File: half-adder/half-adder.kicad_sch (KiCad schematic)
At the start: 14 parts, among them J1 A, J2 B, J3 C, J4 5V, J5 GROUND, J6 CARRY OUT, J7 OUTPUT

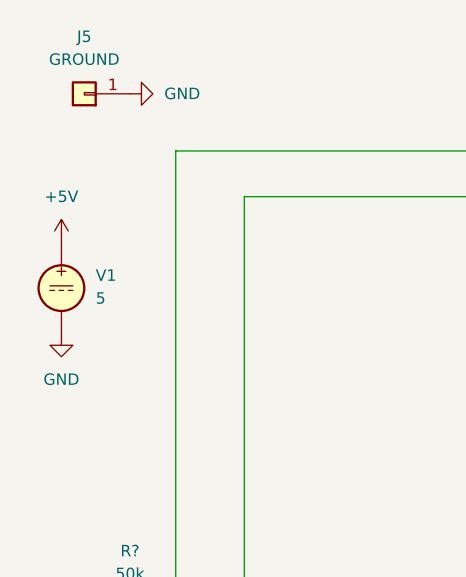
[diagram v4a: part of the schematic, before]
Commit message: complete 2-bit encoder
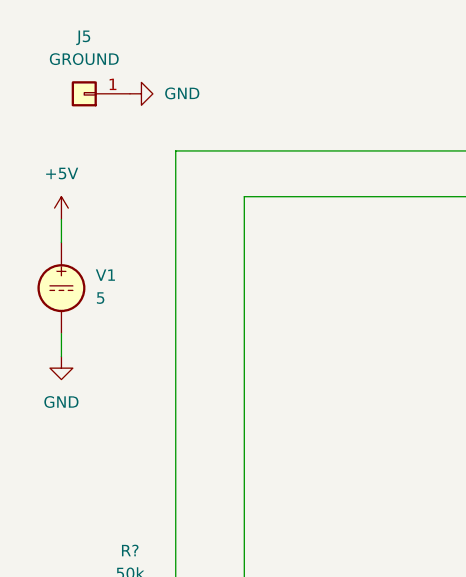
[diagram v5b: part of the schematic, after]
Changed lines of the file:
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@@
+	(wire
+		(pts
+			(xy 17.78 64.77) (xy 17.78 62.23)
+		)
+		(stroke
+			(width 0)
+			(type default)
+		)
+	)
 	(wire
 		(pts
@@
 		(pts
 			(xy 24.13 139.7) (xy 25.4 139.7)
+		)
+		(stroke
+			(width 0)
+			(type default)
+		)
+	)
+	(wire
+		(pts
+			(xy 17.78 49.53) (xy 17.78 52.07)
 		)
 		(stroke
@@
 	(symbol
 		(lib_id "power:+5V")
-		(at 17.78 52.07 0)
+		(at 17.78 49.53 0)
 		(unit 1)
 		(exclude_from_sim no)
@@
 		(fields_autoplaced yes)
 		(property "Reference" "#PWR01"
-			(at 17.78 55.88 0)
+			(at 17.78 53.34 0)
 			(effects
 				(font
@@
 		)
 		(property "Value" "+5V"
-			(at 17.78 46.99 0)
+			(at 17.78 44.45 0)
 			(effects
 				(font
@@
 		)
 		(property "Footprint" ""
-			(at 17.78 52.07 0)
+			(at 17.78 49.53 0)
 			(effects
 				(font
@@
 		)
 		(property "Datasheet" ""
-			(at 17.78 52.07 0)
-			(effects
-				(font
-					(size 1.27 1.27)
-				)
-				(hide yes)
-			)
-		)
-		(property "Description" ""
-			(at 17.78 52.07 0)
+			(at 17.78 49.53 0)
+			(effects
+				(font
+					(size 1.27 1.27)
+				)
+				(hide yes)
+			)
+		)
+		(property "Description" "Power symbol creates a global label with name \"+5V\""
+			(at 17.78 49.53 0)
 			(effects
 				(font
@@
 	)
 	(symbol
-		(lib_name "GND_1")
 		(lib_id "power:GND")
 		(at 25.4 132.08 0)
@@
 			)
 		)
-		(property "Datasheet" "~"
+		(property "Datasheet" "https://ngspice.sourceforge.io/docs/ngspice-html-manual/manual.xhtml#sec_Independent_Sources_for"
 			(at 17.78 57.15 0)
 			(effects
@@
 			)
 		)
-		(property "Description" ""
+		(property "Description" "Voltage source, DC"
 			(at 17.78 57.15 0)
 			(effects
@@
 			)
 		)
-		(property "Description" ""
+		(property "Description" "Power symbol creates a global label with name \"GND\" , ground"
 			(at 50.8 132.08 0)
 			(effects
@@
 			)
 		)
-		(property "Description" ""
+		(property "Description" "Power symbol creates a global label with name \"GND\" , ground"
 			(at 45.72 110.49 0)
 			(effects
@@
 			)
 		)
-		(property "Description" ""
+		(property "Description" "Power symbol creates a global label with name \"GND\" , ground"
 			(at 21.59 92.71 0)
 			(effects
@@
 	)
 	(symbol
-		(lib_name "GND_1")
 		(lib_id "power:GND")
 		(at 25.4 114.3 0)
@@
 	(symbol
 		(lib_id "power:GND")
-		(at 17.78 62.23 0)
+		(at 17.78 64.77 0)
 		(unit 1)
 		(exclude_from_sim no)
@@
 		(fields_autoplaced yes)
 		(property "Reference" "#PWR02"
-			(at 17.78 68.58 0)
+			(at 17.78 71.12 0)
 			(effects
 				(font
@@
 		)
 		(property "Value" "GND"
-			(at 17.78 67.31 0)
+			(at 17.78 69.85 0)
 			(effects
 				(font
@@
 		)
 		(property "Footprint" ""
-			(at 17.78 62.23 0)
+			(at 17.78 64.77 0)
 			(effects
 				(font
@@
 		)
 		(property "Datasheet" ""
-			(at 17.78 62.23 0)
-			(effects
-				(font
-					(size 1.27 1.27)
-				)
-				(hide yes)
-			)
-		)
-		(property "Description" ""
-			(at 17.78 62.23 0)
+			(at 17.78 64.77 0)
+			(effects
+				(font
+					(size 1.27 1.27)
+				)
+				(hide yes)
+			)
+		)
+		(property "Description" "Power symbol creates a global label with name \"GND\" , ground"
+			(at 17.78 64.77 0)
 			(effects
 				(font
@@
 			)
 		)
-		(property "Description" ""
+		(property "Description" "Power symbol creates a global label with name \"+5V\""
 			(at 25.4 22.86 0)
 			(effects
@@
 			)
 		)
-		(property "Description" ""
+		(property "Description" "Power symbol creates a global label with name \"+5V\""
 			(at 128.27 21.59 0)
 			(effects
@@
 			)
 		)
-		(property "Description" ""
+		(property "Description" "Special symbol for telling ERC where power comes from"
 			(at 128.27 21.59 0)
 			(effects
@@
 			)
 		)
-		(property "Description" ""
+		(property "Description" "Special symbol for telling ERC where power comes from"
 			(at 142.24 21.59 0)
 			(effects
@@
 	)
 	(symbol
-		(lib_name "GND_1")
 		(lib_id "power:GND")
 		(at 25.4 152.4 0)
@@
 			)
 		)
-		(property "Description" ""
+		(property "Description" "Power symbol creates a global label with name \"GND\" , ground"
 			(at 142.24 21.59 0)
 			(effects
@@
 			)
 		)
-		(property "Description" ""
+		(property "Description" "Power symbol creates a global label with name \"GND\" , ground"
 			(at 25.4 35.56 0)
 			(effects

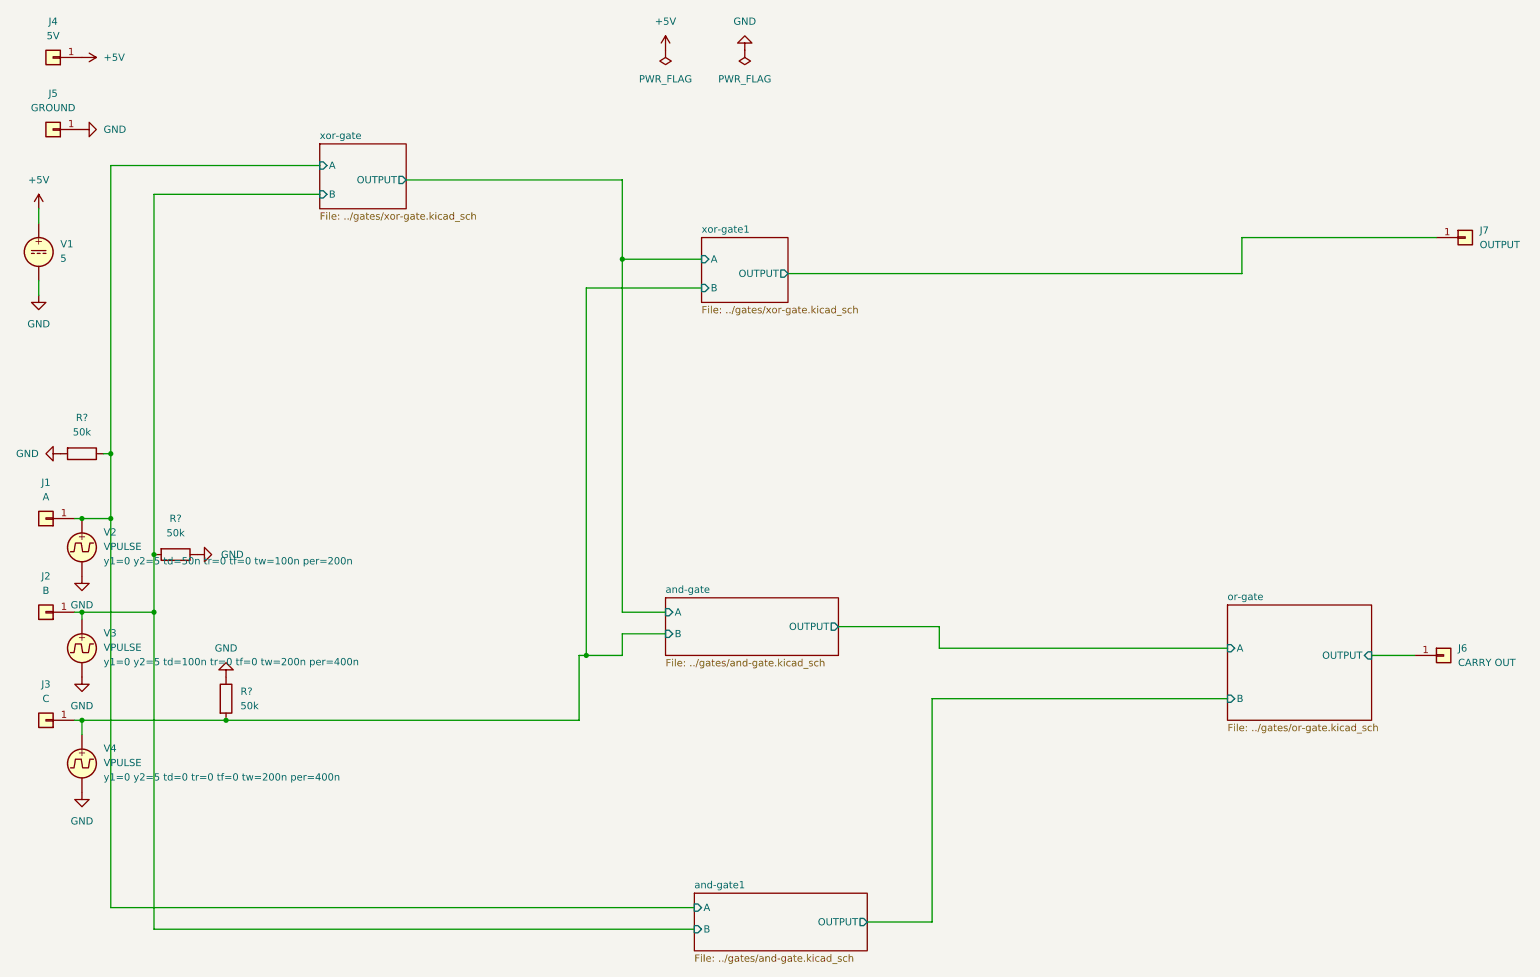
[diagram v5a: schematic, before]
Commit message: Use IC circuits in adder circuit
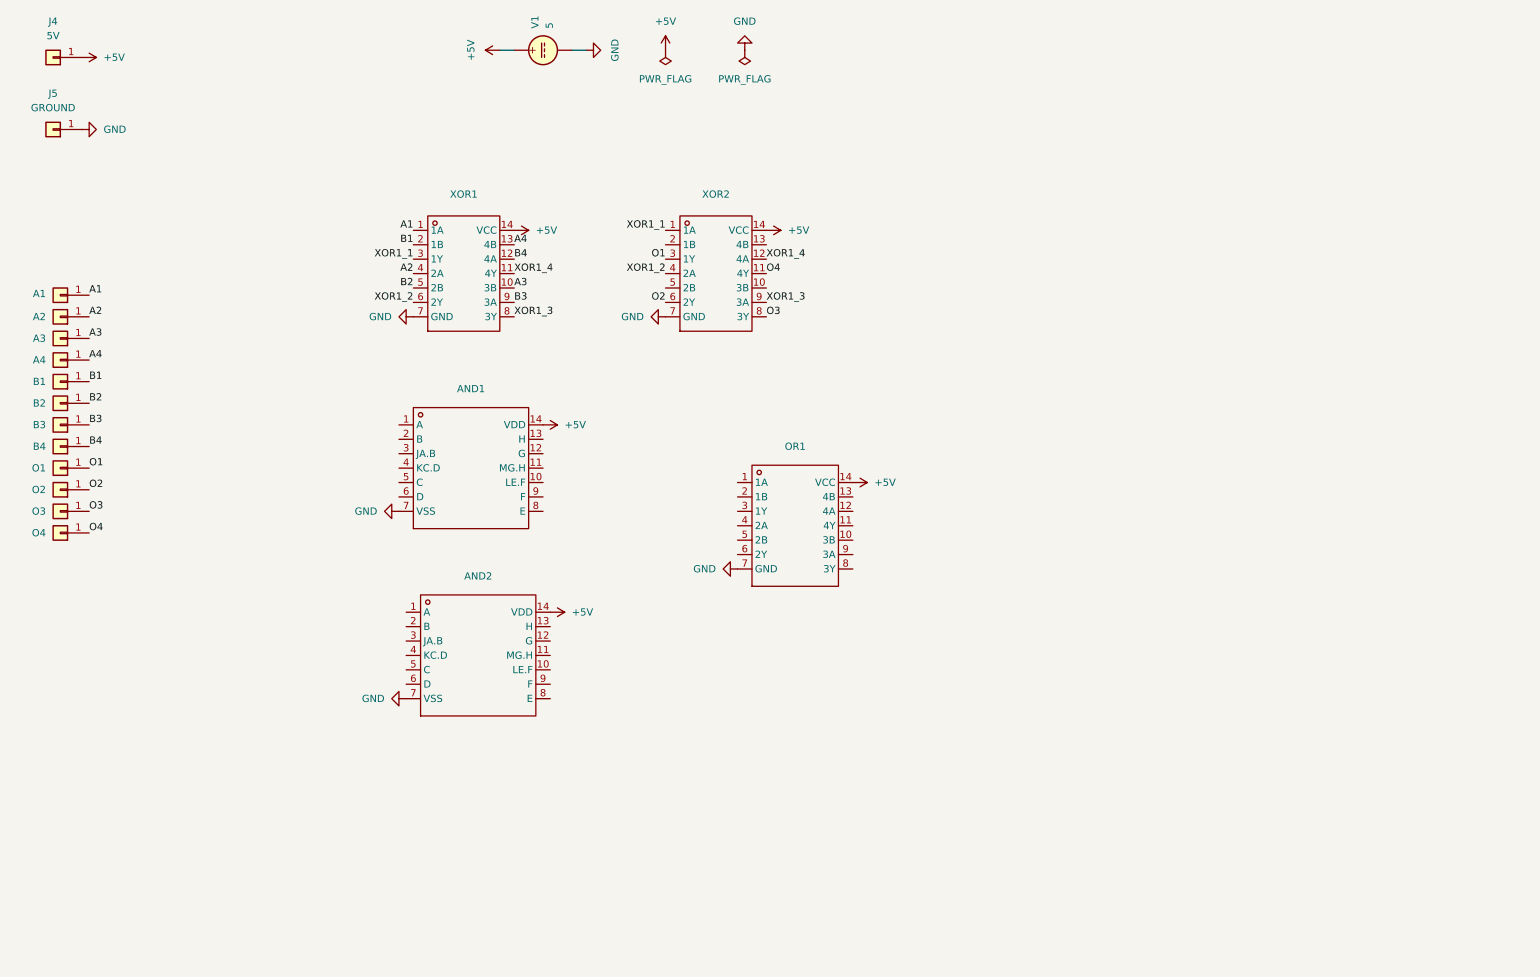
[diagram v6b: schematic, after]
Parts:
- removed J1: A, Connector_PinHeader_2.54mm:PinHeader_1x01_P2.54mm_Vertical, symbol Connector_Generic:Conn_01x01
- removed J2: B, Connector_PinHeader_2.54mm:PinHeader_1x01_P2.54mm_Vertical, symbol Connector_Generic:Conn_01x01
- removed J3: C, Connector_PinHeader_2.54mm:PinHeader_1x01_P2.54mm_Vertical, symbol Connector_Generic:Conn_01x01
- removed J6: CARRY OUT, Connector_PinHeader_2.54mm:PinHeader_1x01_P2.54mm_Vertical, symbol Connector_Generic:Conn_01x01
- removed J7: OUTPUT, Connector_PinHeader_2.54mm:PinHeader_1x01_P2.54mm_Vertical, symbol Connector_Generic:Conn_01x01
- removed R? (x3): 50k, R0603:R0603, symbol Device:R
- removed V2, V3, V4: VPULSE, symbol Simulation_SPICE:VPULSE
- added A1, A2, A3, A4, B1, B2, B3, B4, O1, O2, O3, O4: ~, Connector_PinHeader_2.54mm:PinHeader_1x01_P2.54mm_Vertical, symbol Connector_Generic:Conn_01x01
- added AND1, AND2: ~, easyeda:PDIP-14_L19.3-W6.4-P2.54-LS7.6-BL, symbol easyeda:CD4081BE
- added OR1: ~, easyeda:DIP-14_L19.0-W7.0-P2.54-LS7.6-BL, symbol easyeda:SN74HC32N
- added XOR1, XOR2: ~, easyeda:SOIC-14_L8.7-W3.9-P1.27-LS6.0-BL, symbol easyeda:74HC86D
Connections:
- net +5V: now also AND1.14 (VDD), AND2.14 (VDD), OR1.14 (VCC), XOR1.14 (VCC), XOR2.14 (VCC)
- net GND: now also AND1.7 (VSS), AND2.7 (VSS), OR1.7 (GND), XOR1.7 (GND), XOR2.7 (GND)
- new net A1: A1.1 (Pin_1), XOR1.1 (1A)
- new net A2: A2.1 (Pin_1), XOR1.4 (2A)
- new net A3: A3.1 (Pin_1), XOR1.10 (3B)
- new net A4: A4.1 (Pin_1), XOR1.13 (4B)
- new net B1: B1.1 (Pin_1), XOR1.2 (1B)
- new net B2: B2.1 (Pin_1), XOR1.5 (2B)
- new net B3: B3.1 (Pin_1), XOR1.9 (3A)
- new net B4: B4.1 (Pin_1), XOR1.12 (4A)
- new net O1: O1.1 (Pin_1), XOR2.3 (1Y)
- new net O2: O2.1 (Pin_1), XOR2.6 (2Y)
- new net O3: O3.1 (Pin_1), XOR2.8 (3Y)
- new net O4: O4.1 (Pin_1), XOR2.11 (4Y)
- new net XOR1_1: XOR1.3 (1Y), XOR2.1 (1A)
- new net XOR1_2: XOR1.6 (2Y), XOR2.4 (2A)
- new net XOR1_3: XOR1.8 (3Y), XOR2.9 (3A)
- new net XOR1_4: XOR1.11 (4Y), XOR2.12 (4A)
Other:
- removed sheet and-gate
- removed sheet and-gate1
- removed sheet or-gate
- removed sheet xor-gate
- removed sheet xor-gate1
- moved on the sheet: V1
